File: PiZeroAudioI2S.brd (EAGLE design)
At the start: 65.1 x 30.2 mm, 69 parts, among them CON1 RPI-ZERO, J1 GROVE, J2 2X2HEADER, J3 2X1-LOCKING, J4 GROVE, J5 4X1-LOCKING, Q1 DMG2305UX, U1 TXB0104PWR, U2 LSM6DS33, U3 PCM5101A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

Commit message: changed component values so they are consistent
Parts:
- C1, C17, C2, C32, C6: value 100nF -> 0.1uF
- C33: value 100UF -> 100uF
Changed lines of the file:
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@@
 <attribute name="NAME" x="-61.8874" y="22.733" size="0.6096" layer="25" font="vector" ratio="20" rot="R270" align="bottom-center"/>
 </element>
-<element name="C6" library="rcl" library_urn="urn:adsk.eagle:library:334" package="C0603" package3d_urn="urn:adsk.eagle:package:23616/2" value="100nF" x="-70.3786" y="23.5712" smashed="yes">
+<element name="C6" library="rcl" library_urn="urn:adsk.eagle:library:334" package="C0603" package3d_urn="urn:adsk.eagle:package:23616/2" value="0.1uF" x="-70.3786" y="23.5712" smashed="yes">
 <attribute name="NAME" x="-70.0024" y="22.606" size="0.8128" layer="25" rot="R180"/>
 <attribute name="SPICEPREFIX" value="C" x="-70.3786" y="23.5712" size="1.778" layer="27" display="off"/>
 </element>
-<element name="C1" library="rcl" library_urn="urn:adsk.eagle:library:334" package="C0603" package3d_urn="urn:adsk.eagle:package:23616/2" value="100nF" x="-42.1894" y="23.2156" smashed="yes" rot="R90">
+<element name="C1" library="rcl" library_urn="urn:adsk.eagle:library:334" package="C0603" package3d_urn="urn:adsk.eagle:package:23616/2" value="0.1uF" x="-42.1894" y="23.2156" smashed="yes" rot="R90">
 <attribute name="NAME" x="-41.529" y="22.1234" size="0.8128" layer="25" rot="R180"/>
 <attribute name="SPICEPREFIX" value="C" x="-42.1894" y="23.2156" size="1.778" layer="27" rot="R90" display="off"/>
@@
 <attribute name="NAME" x="-57.531" y="23.6474" size="0.8128" layer="25" rot="R180"/>
 </element>
-<element name="C2" library="rcl" library_urn="urn:adsk.eagle:library:334" package="C0603" package3d_urn="urn:adsk.eagle:package:23616/2" value="100nF" x="-73.279" y="22.479" smashed="yes" rot="R90">
+<element name="C2" library="rcl" library_urn="urn:adsk.eagle:library:334" package="C0603" package3d_urn="urn:adsk.eagle:package:23616/2" value="0.1uF" x="-73.279" y="22.479" smashed="yes" rot="R90">
 <attribute name="NAME" x="-72.898" y="24.3332" size="0.8128" layer="25" rot="R180"/>
 <attribute name="SPICEPREFIX" value="C" x="-73.279" y="22.479" size="1.778" layer="27" rot="R90" display="off"/>
@@
 <attribute name="NAME" x="-52.9082" y="5.207" size="0.8128" layer="25" font="vector" ratio="15"/>
 </element>
-<element name="C17" library="rcl" library_urn="urn:adsk.eagle:library:334" package="C0603" package3d_urn="urn:adsk.eagle:package:23616/2" value="100nF" x="-58.801" y="3.7721" smashed="yes" rot="R270">
+<element name="C17" library="rcl" library_urn="urn:adsk.eagle:library:334" package="C0603" package3d_urn="urn:adsk.eagle:package:23616/2" value="0.1uF" x="-58.801" y="3.7721" smashed="yes" rot="R270">
 <attribute name="NAME" x="-60.071" y="2.8731" size="0.8128" layer="25" rot="R180"/>
 <attribute name="SPICEPREFIX" value="C" x="-58.801" y="3.7721" size="1.778" layer="27" rot="R270" display="off"/>
@@
 <attribute name="NAME" x="-48.641" y="20.32" size="0.8128" layer="25" rot="R180"/>
 </element>
-<element name="C32" library="rcl" library_urn="urn:adsk.eagle:library:334" package="C0603" package3d_urn="urn:adsk.eagle:package:23616/2" value="100nF" x="-59.3344" y="18.1864" smashed="yes" rot="R90">
+<element name="C32" library="rcl" library_urn="urn:adsk.eagle:library:334" package="C0603" package3d_urn="urn:adsk.eagle:package:23616/2" value="0.1uF" x="-59.3344" y="18.1864" smashed="yes" rot="R90">
 <attribute name="NAME" x="-62.484" y="18.7452" size="0.8128" layer="25"/>
 <attribute name="SPICEPREFIX" value="C" x="-59.3344" y="18.1864" size="1.778" layer="27" rot="R90" display="off"/>
 </element>
-<element name="C33" library="HappyBrackets" library_urn="urn:adsk.eagle:library:5224691" package="0603-POLAR" value="100UF" x="-69.0118" y="19.5834" smashed="yes" rot="R180">
+<element name="C33" library="HappyBrackets" library_urn="urn:adsk.eagle:library:5224691" package="0603-POLAR" value="100uF" x="-69.0118" y="19.5834" smashed="yes" rot="R180">
 <attribute name="NAME" x="-68.0974" y="18.7198" size="0.8128" layer="25" rot="R180"/>
 </element>

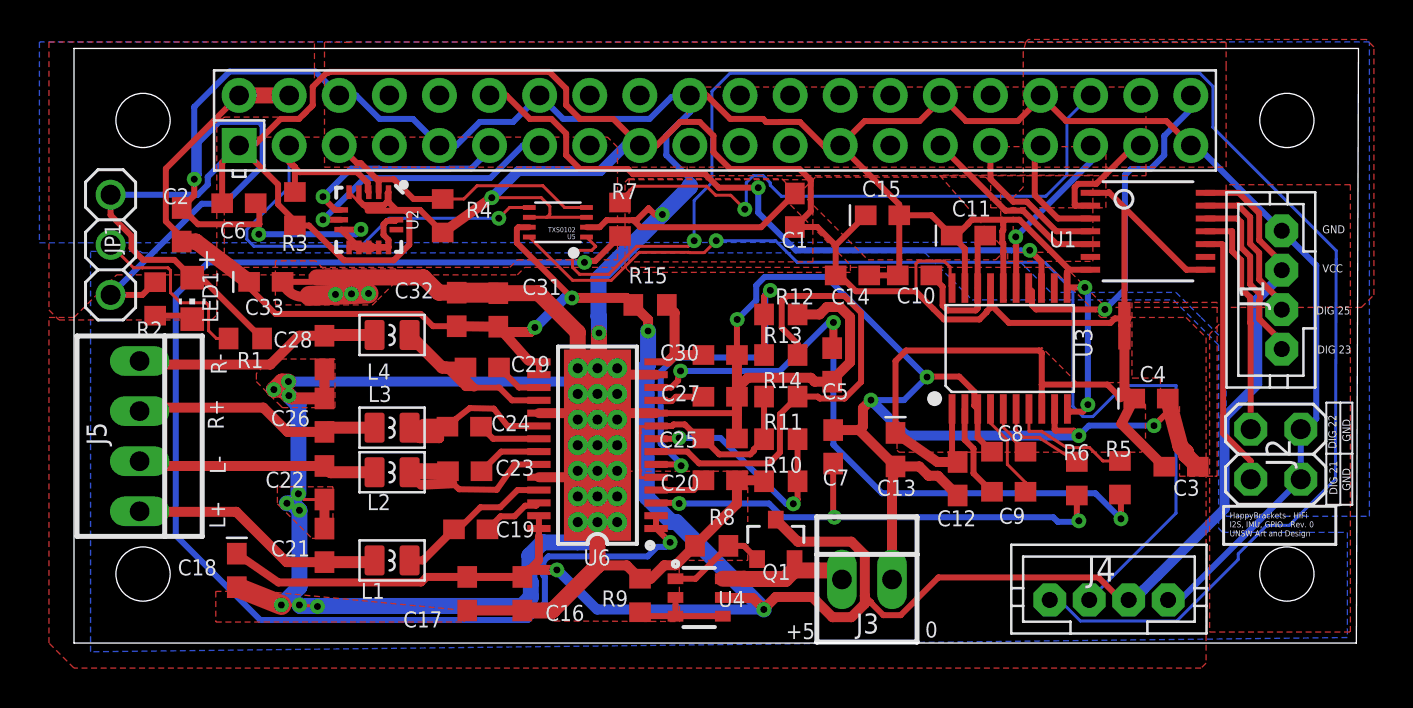
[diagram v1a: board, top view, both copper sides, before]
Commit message: Changed Capacitor sizes for tant caps
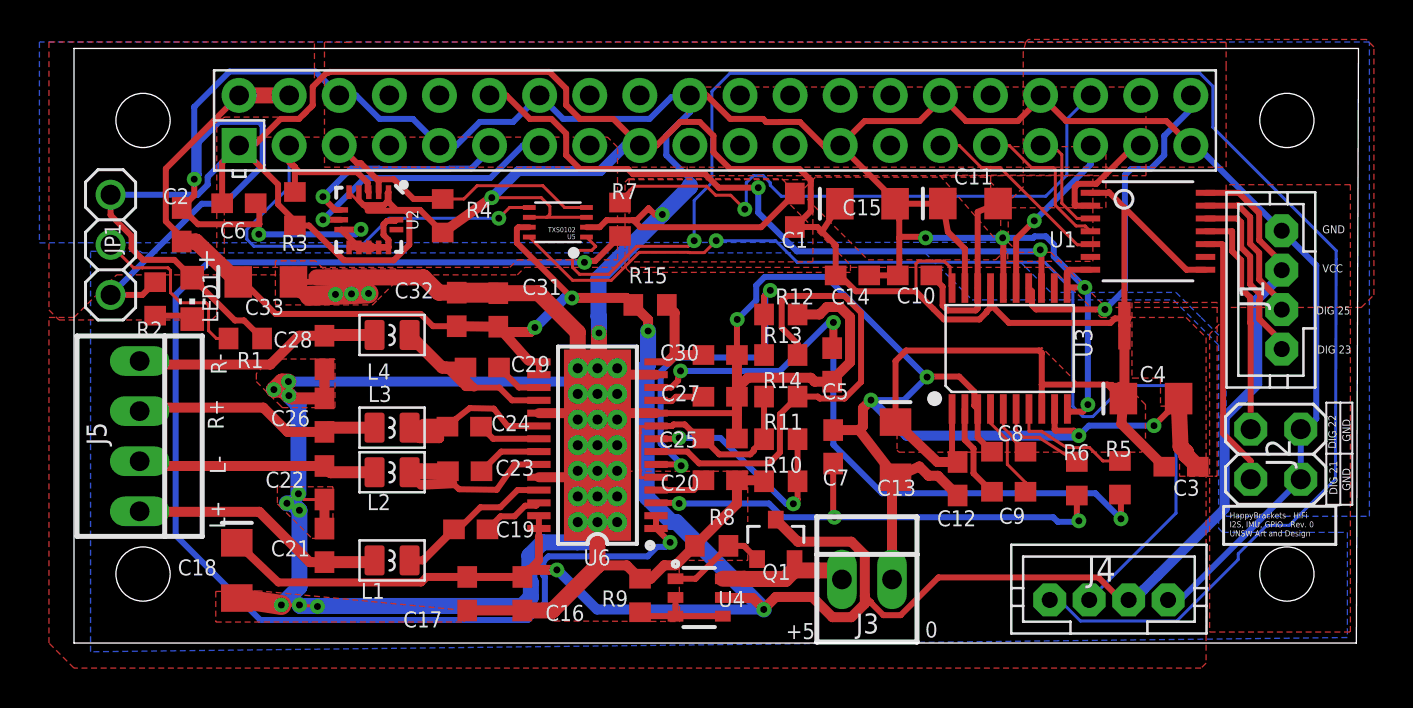
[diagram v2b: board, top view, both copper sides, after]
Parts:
- C11, C13, C15, C18, C33, C4: device HappyBrackets:0603-POLAR -> HappyBrackets:EIA3216
- moved C11 1.63 mm to (-33.3, 23.6)
- moved C15 0.96 mm to (-38.5, 23.5)
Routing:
- net GND: track 200.1 -> 204.7 mm, vias 7 -> 9
- net N$12: track 7.54 -> 9.70 mm
- net AGND: track 270.2 -> 268.6 mm
- net AN3V3: track 33.1 -> 32.2 mm

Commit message: Added gnd to SCK pin
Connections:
- net GND: now also U3.12
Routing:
- net GND: track 204.7 -> 205.5 mm
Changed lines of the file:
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@@
 <vertex x="-13.0556" y="31.75"/>
 </polygon>
-<wire x1="-52.1462" y1="15.7226" x2="-52.1208" y2="15.748" width="0.8128" layer="1"/>
 <wire x1="-52.1208" y1="15.748" x2="-52.1208" y2="16.9926" width="0.8128" layer="1"/>
 <via x="-52.1208" y="16.9926" extent="1-16" drill="0.35"/>
@@
 <wire x1="-72.644" y1="24.7904" x2="-72.644" y2="23.964" width="0.3048" layer="1"/>
 <wire x1="-72.644" y1="23.964" x2="-73.279" y2="23.329" width="0.3048" layer="1"/>
-<wire x1="-52.1462" y1="17.8308" x2="-52.1462" y2="17.8308" width="0.8128" layer="16"/>
 <wire x1="-48.44570625" y1="28.956" x2="-47.51" y2="28.956" width="0.3048" layer="16"/>
 <wire x1="-49.55550625" y1="27.8462" x2="-48.44570625" y2="28.956" width="0.3048" layer="16"/>
@@
 <wire x1="-55.13" y1="29.04" x2="-53.9362" y2="27.8462" width="0.3048" layer="16"/>
 <wire x1="-64.2924" y1="21.333" x2="-63.6778" y2="21.333" width="0.508" layer="1"/>
+<wire x1="-64.7924" y1="21.333" x2="-64.2924" y2="21.333" width="0.3048" layer="1"/>
 <wire x1="-63.7924" y1="21.333" x2="-63.6778" y2="21.333" width="0.3048" layer="1"/>
-<wire x1="-64.7924" y1="21.333" x2="-64.2924" y2="21.333" width="0.3048" layer="1"/>
-<wire x1="-63.7924" y1="21.333" x2="-63.3476" y2="21.333" width="0.3048" layer="1"/>
 <wire x1="-63.2924" y1="21.333" x2="-62.7924" y2="21.333" width="0.3048" layer="1"/>
 <wire x1="-65.1924" y1="22.233" x2="-64.27" y2="22.233" width="0.3048" layer="1"/>
@@
 <wire x1="-69.3674" y1="22.479" x2="-69.342" y2="22.5044" width="0.3048" layer="1"/>
 <wire x1="-64.4398" y1="21.9964" x2="-69.3674" y2="21.9964" width="0.3048" layer="16"/>
-<wire x1="-52.2478" y1="15.621" x2="-52.1462" y2="15.7226" width="0.8128" layer="1"/>
+<wire x1="-52.2478" y1="15.621" x2="-52.1208" y2="15.748" width="0.8128" layer="1"/>
 <wire x1="-52.1208" y1="17.8054" x2="-52.1462" y2="17.8308" width="0.8128" layer="16"/>
 <polygon width="0.1524" layer="1">
@@
 <wire x1="-28.3828" y1="20.0516" x2="-28.3828" y2="19.2702" width="0.3048" layer="1"/>
 <wire x1="-36.8944" y1="23.624125" x2="-37.1064" y2="23.5458" width="0.3048" layer="1"/>
-<wire x1="-36.8944" y1="23.624125" x2="-36.8944" y2="22.7584" width="0.3048" layer="1"/>
+<wire x1="-36.8944" y1="23.624125" x2="-36.8944" y2="23.5044" width="0.3048" layer="1"/>
 <wire x1="-36.8944" y1="19.988" x2="-36.9688" y2="19.9136" width="0.3048" layer="1"/>
 <wire x1="-36.9688" y1="19.9136" x2="-38.4184" y2="19.9136" width="0.3048" layer="1"/>
@@
 <wire x1="-35.613596875" y1="21.8694" x2="-35.56" y2="21.815803125" width="0.3048" layer="1"/>
 <via x="-35.56" y="21.815803125" extent="1-16" drill="0.35"/>
-<wire x1="-35.56" y1="21.815803125" x2="-31.623" y2="21.815803125" width="0.3048" layer="16"/>
+<wire x1="-35.56" y1="21.815803125" x2="-31.650796875" y2="21.815803125" width="0.3048" layer="16"/>
 <wire x1="-31.623" y1="21.815803125" x2="-30.102509375" y2="21.815803125" width="0.3048" layer="16"/>
 <wire x1="-30.102509375" y1="21.815803125" x2="-30.0263125" y2="21.892" width="0.3048" layer="16"/>
@@
 <wire x1="-31.6508" y1="21.8158" x2="-31.650796875" y2="21.815803125" width="0.3048" layer="16"/>
 <wire x1="-31.650796875" y1="21.815803125" x2="-31.623" y2="21.815803125" width="0.3048" layer="16"/>
+<contactref element="U3" pad="12"/>
+<wire x1="-29.0328" y1="19.2702" x2="-29.0328" y2="20.3194" width="0.1524" layer="1"/>
+<wire x1="-29.0328" y1="20.3194" x2="-28.8798" y2="20.4724" width="0.1524" layer="1"/>
+<wire x1="-28.8798" y1="20.4724" x2="-28.6062" y2="20.1988" width="0.1524" layer="1"/>
+<wire x1="-28.6062" y1="20.1988" x2="-28.2644" y2="20.1988" width="0.1524" layer="1"/>
 </signal>
 <signal name="PCM_FS">
